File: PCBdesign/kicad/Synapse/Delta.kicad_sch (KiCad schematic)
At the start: 12 parts, among them IC1 ALD1105PBL, P4 TSW-102-07-G-S

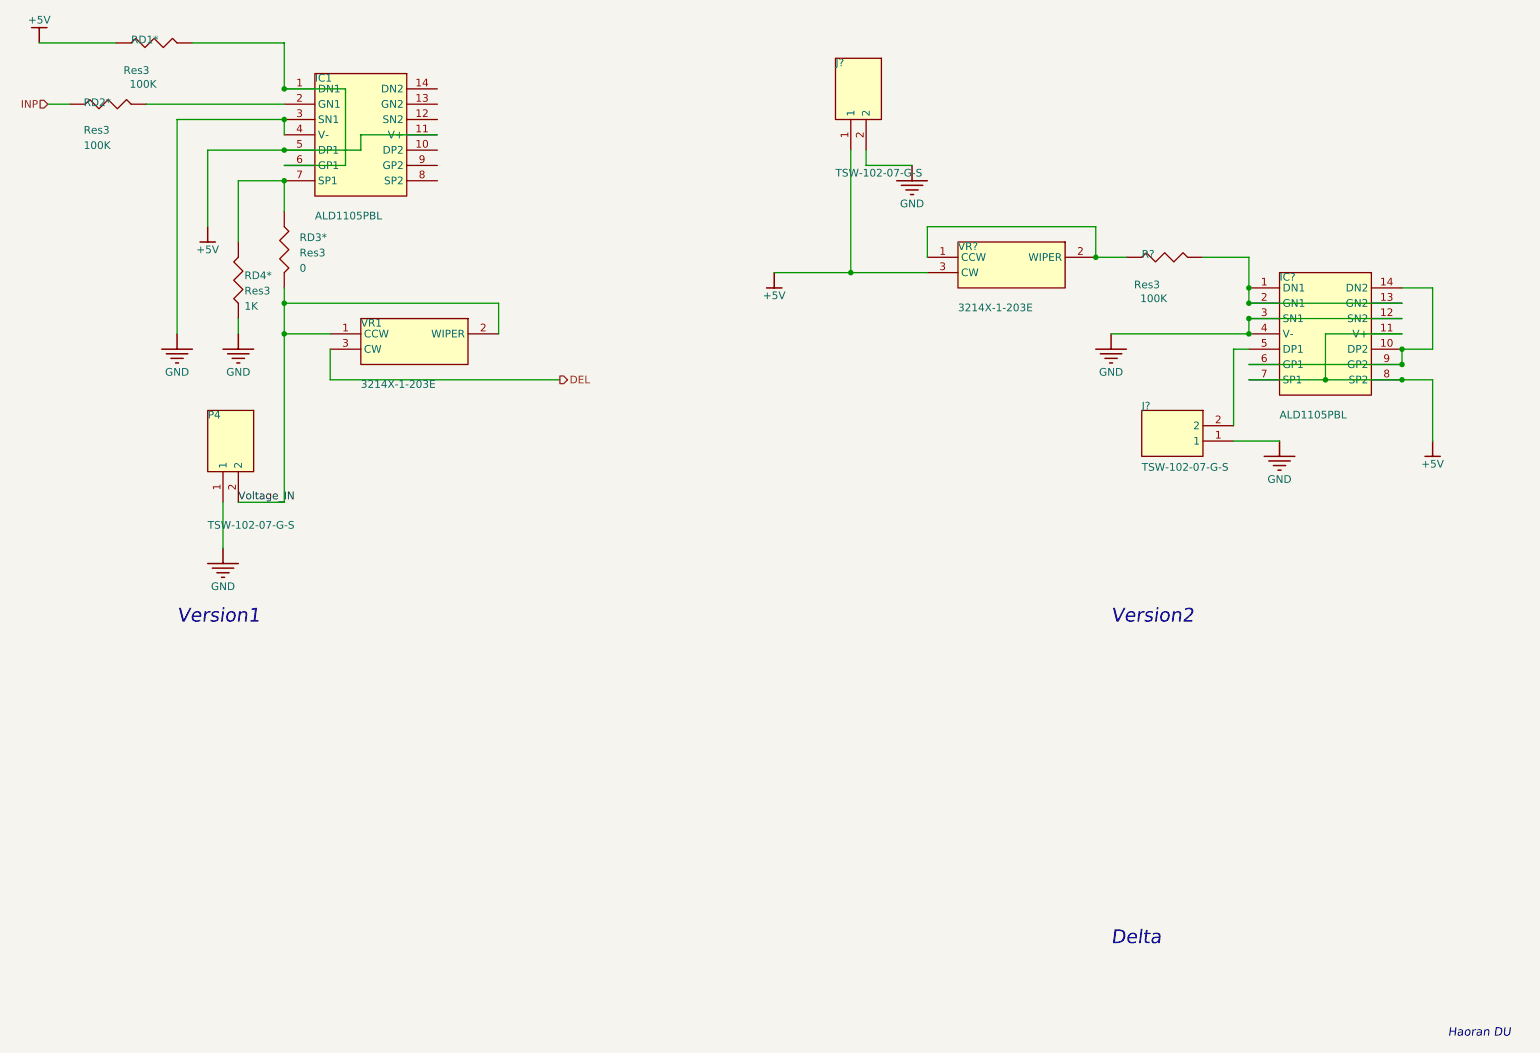
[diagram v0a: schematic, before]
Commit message: Replace ALD component with BJTs in Delta
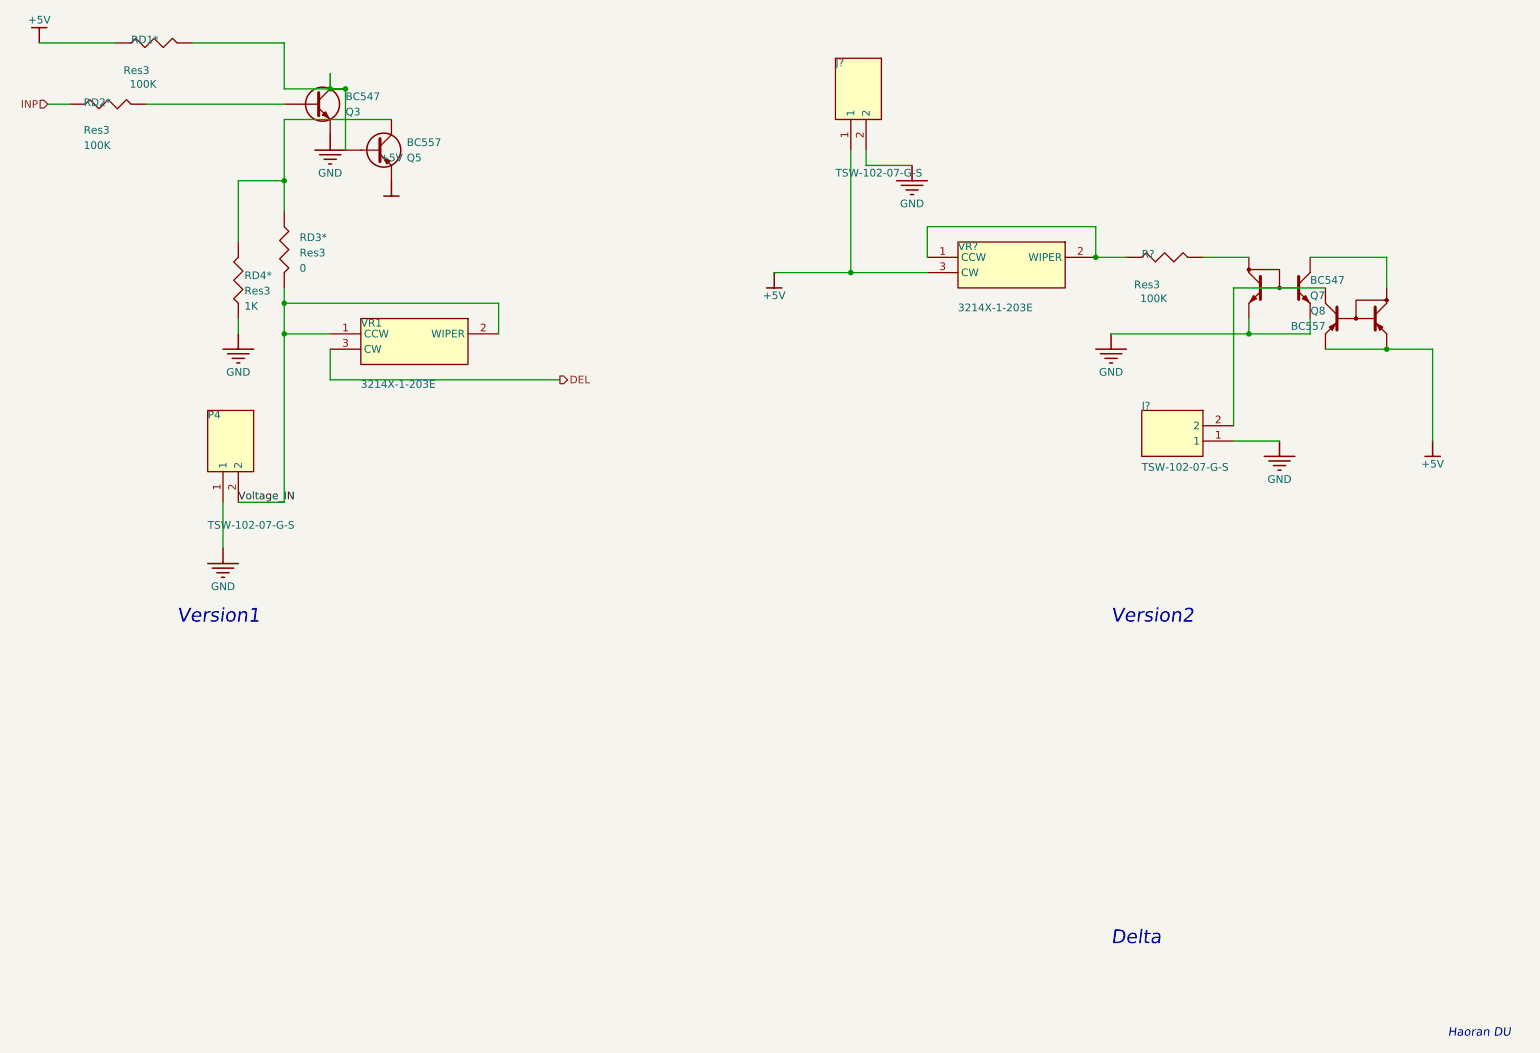
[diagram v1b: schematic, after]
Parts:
- removed IC1, IC?: ALD1105PBL, C__Users_86135_Documents_AltiumLL_SamacSys.PcbLib:DIP762W51P254L1828H508Q14N, symbol *:0_0_ALD1105PBL_*
- added Q3: BC547, symbol Device:Q_NPN
- added Q5: BC557, symbol Device:Q_PNP
- added Q7: BC547, symbol Device:Q_NPN_CurrentMirror
- added Q8: BC557, symbol Device:Q_PNP_CurrentMirror
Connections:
- net +5V: now also Q5.E, Q8.E1, Q8.E2
- net GND: now also Q3.E, Q7.E1, Q7.E2
- net at RD1*.2: now also Q3.C, Q5.B
- net at RD3*.1, RD4*.2: now also Q5.C
- net at R?.2: now also Q7.C2
- net at J?.2: now also Q8.C1
- net at RD2*.2: now also Q3.B
- new net: Q7.C1, Q8.C2

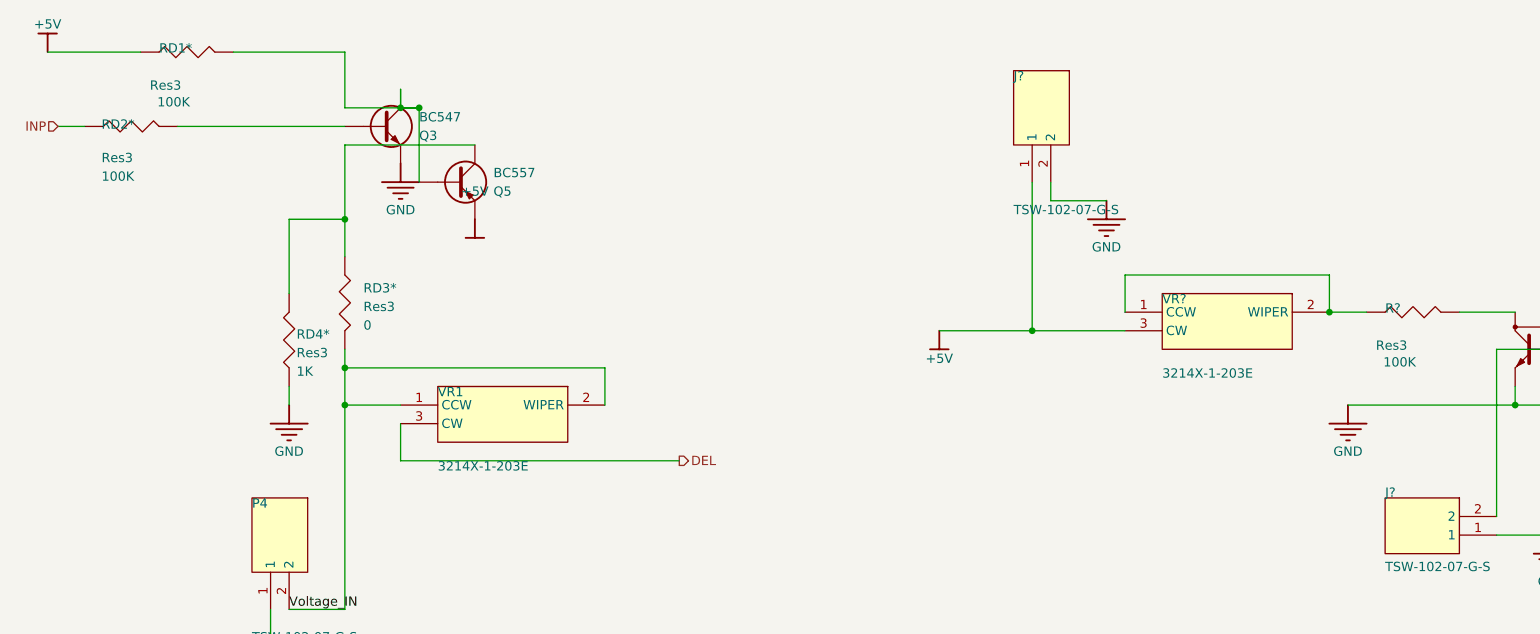
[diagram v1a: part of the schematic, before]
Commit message: Add annotation script, wiring checklist for breadboarding, and .gitignore in case proprietary libs are added. Fix annotations that were missing after KiCad import in the schematics.
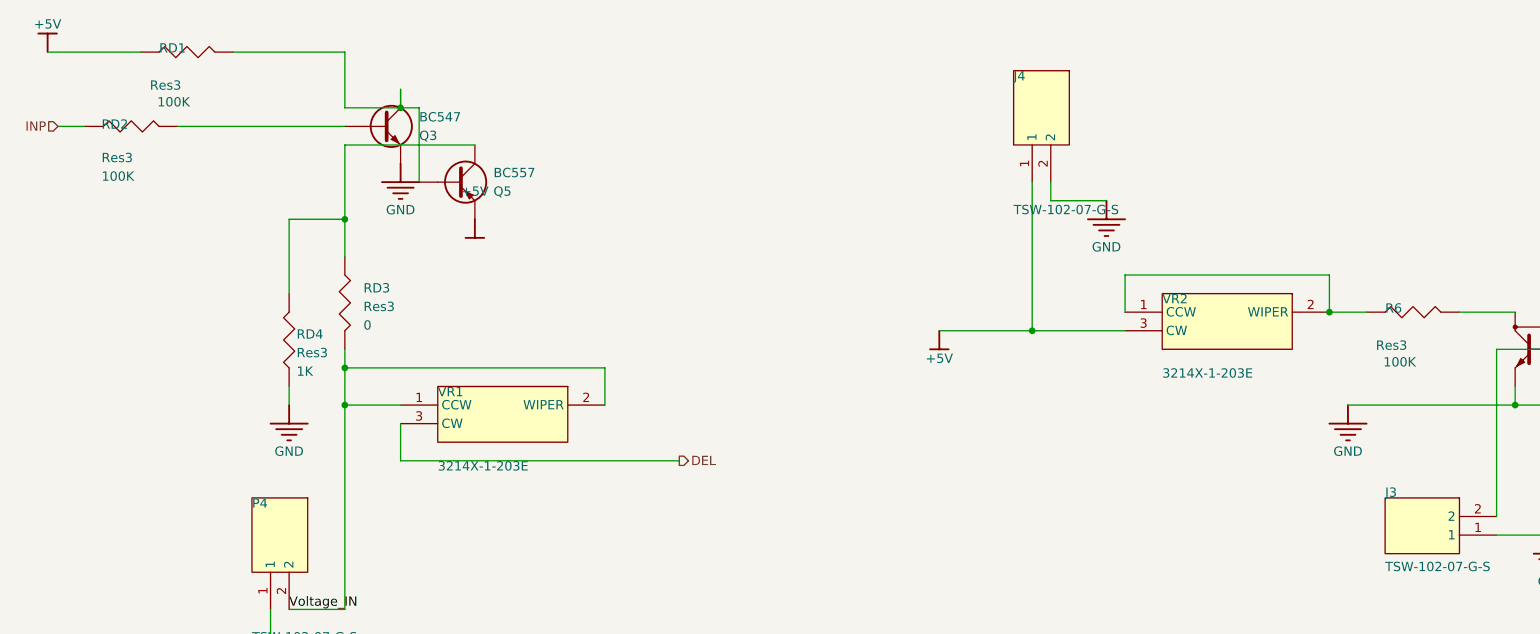
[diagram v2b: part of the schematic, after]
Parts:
- gave numbers to parts that had none: 4
- renumbered RD1* to RD1, RD2* to RD2, RD3* to RD3, RD4* to RD4
